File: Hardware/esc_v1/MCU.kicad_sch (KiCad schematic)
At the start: 28 parts, among them SW1 SW_Push, U4 ATSAME70J21A-AN, Y1 Crystal_GND2

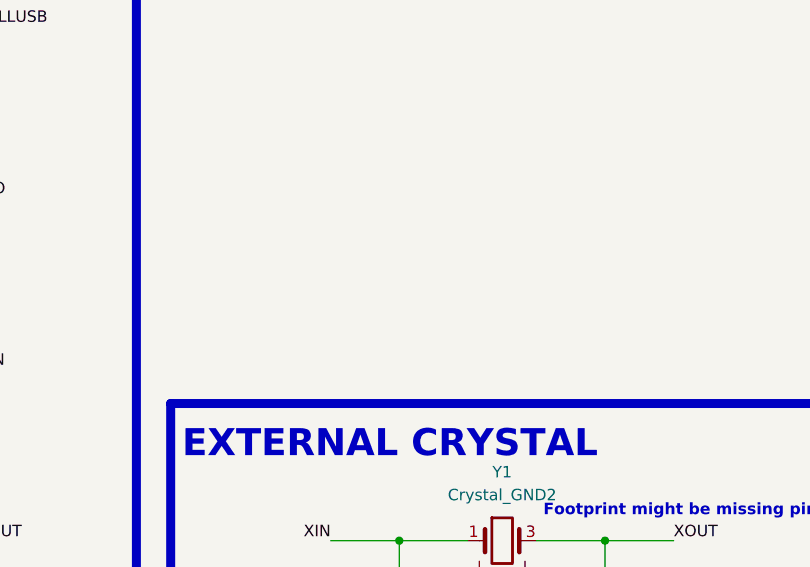
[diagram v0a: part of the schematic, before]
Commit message: changed gate driver, removed 10V buck and 5V LDO, added 5V buck. Started on Layout
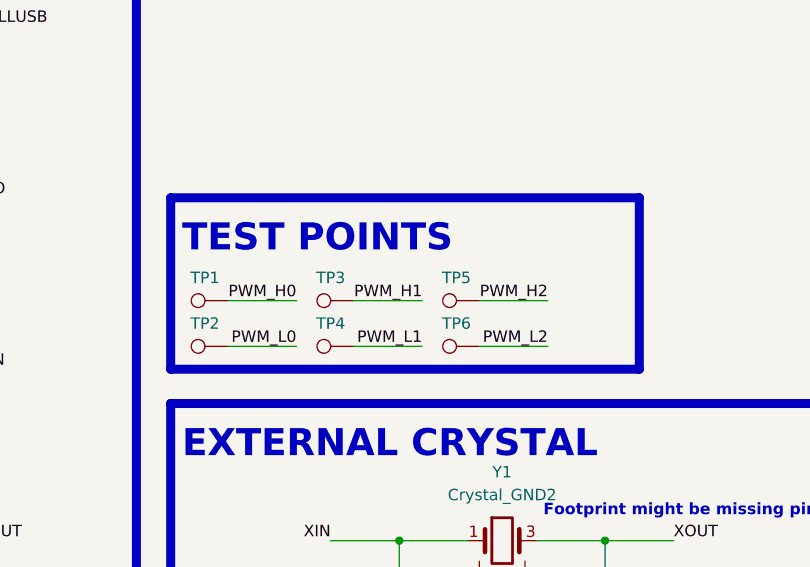
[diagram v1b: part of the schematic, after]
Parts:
- added TP1, TP2, TP3, TP4, TP5, TP6: TestPoint, TestPoint:TestPoint_Pad_D3.0mm, symbol Connector:TestPoint
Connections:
- net PWM_H0: now also TP1.1
- net PWM_H1: now also TP3.1
- net PWM_H2: now also TP5.1
- net PWM_L0: now also TP2.1
- net PWM_L1: now also TP4.1
- net PWM_L2: now also TP6.1
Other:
- note added: "TEST POINTS"
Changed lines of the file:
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@@
   (title_block
     (title "MCU")
-    (date "2022-07-21")
+    (date "2022-08-13")
     (rev "1")
   )
@@
     (stroke (width 0) (type default) (color 0 0 0 0))
   )
+  (wire (pts (xy 120.65 113.03) (xy 128.27 113.03))
+    (stroke (width 0) (type default) (color 0 0 0 0))
+  )
   (polyline (pts (xy 147.32 163.83) (xy 147.32 195.58))
     (stroke (width 1) (type solid) (color 0 0 0 0))
@@
     (stroke (width 1) (type solid) (color 0 0 0 0))
   )
+  (wire (pts (xy 134.62 118.11) (xy 142.24 118.11))
+    (stroke (width 0) (type default) (color 0 0 0 0))
+  )
   (wire (pts (xy 64.77 158.75) (xy 72.39 158.75))
     (stroke (width 0) (type default) (color 0 0 0 0))
@@
     (stroke (width 0) (type default) (color 0 0 0 0))
   )
+  (wire (pts (xy 106.68 113.03) (xy 114.3 113.03))
+    (stroke (width 0) (type default) (color 0 0 0 0))
+  )
   (polyline (pts (xy 48.26 13.97) (xy 96.52 13.97))
     (stroke (width 1) (type solid) (color 0 0 0 0))
@@
     (stroke (width 1) (type solid) (color 0 0 0 0))
   )
+  (polyline (pts (xy 152.4 120.65) (xy 100.33 120.65))
+    (stroke (width 1) (type solid) (color 0 0 0 0))
+  )
   (wire (pts (xy 73.66 34.29) (xy 74.93 34.29))
     (stroke (width 0) (type default) (color 0 0 0 0))
@@
     (stroke (width 0) (type default) (color 0 0 0 0))
   )
+  (polyline (pts (xy 152.4 101.6) (xy 100.33 101.6))
+    (stroke (width 1) (type solid) (color 0 0 0 0))
+  )
   (polyline (pts (xy 13.97 74.93) (xy 13.97 195.58))
     (stroke (width 1) (type solid) (color 0 0 0 0))
@@
     (stroke (width 0) (type default) (color 0 0 0 0))
   )
+  (wire (pts (xy 134.62 113.03) (xy 142.24 113.03))
+    (stroke (width 0) (type default) (color 0 0 0 0))
+  )
   (wire (pts (xy 118.11 139.7) (xy 125.73 139.7))
     (stroke (width 0) (type default) (color 0 0 0 0))
@@
     (stroke (width 0) (type default) (color 0 0 0 0))
   )
+  (wire (pts (xy 106.68 118.11) (xy 114.3 118.11))
+    (stroke (width 0) (type default) (color 0 0 0 0))
+  )
   (wire (pts (xy 49.53 139.7) (xy 64.77 139.7))
     (stroke (width 0) (type default) (color 0 0 0 0))
@@
     (stroke (width 1) (type solid) (color 0 0 0 0))
   )
+  (polyline (pts (xy 152.4 101.6) (xy 152.4 120.65))
+    (stroke (width 1) (type solid) (color 0 0 0 0))
+  )
   (wire (pts (xy 72.39 101.6) (xy 76.2 101.6))
     (stroke (width 0) (type default) (color 0 0 0 0))
@@
     (stroke (width 0) (type default) (color 0 0 0 0))
   )
+  (polyline (pts (xy 100.33 101.6) (xy 100.33 120.65))
+    (stroke (width 1) (type solid) (color 0 0 0 0))
+  )
   (wire (pts (xy 130.81 186.69) (xy 130.81 190.5))
     (stroke (width 0) (type default) (color 0 0 0 0))
@@
   )
   (wire (pts (xy 196.85 83.82) (xy 209.55 83.82))
+    (stroke (width 0) (type default) (color 0 0 0 0))
+  )
+  (wire (pts (xy 120.65 118.11) (xy 128.27 118.11))
     (stroke (width 0) (type default) (color 0 0 0 0))
   )
@@
     (effects (font (size 3 3) (thickness 0.6) bold) (justify left bottom))
   )
+  (text "TEST POINTS" (at 101.6 107.95 0)
+    (effects (font (size 3 3) (thickness 0.6) bold) (justify left bottom))
+  )
   (text "Footprint might be missing pin 4" (at 173.99 137.16 180)
     (effects (font (size 1.27 1.27) (thickness 0.254) bold) (justify right bottom))
@@
     (effects (font (size 1.27 1.27)) (justify left bottom))
   )
+  (label "PWM_H1" (at 128.27 113.03 180)
+    (effects (font (size 1.27 1.27)) (justify right bottom))
+  )
   (label "XOUT" (at 196.85 104.14 0)
     (effects (font (size 1.27 1.27)) (justify left bottom))
@@
     (effects (font (size 1.27 1.27)) (justify left bottom))
   )
+  (label "PWM_L2" (at 142.24 118.11 180)
+    (effects (font (size 1.27 1.27)) (justify right bottom))
+  )
   (label "VDDPLL" (at 242.57 30.48 0)
     (effects (font (size 1.27 1.27)) (justify left bottom))
@@
   (label "VDDIO" (at 227.33 20.32 0)
     (effects (font (size 1.27 1.27)) (justify left bottom))
+  )
+  (label "PWM_L0" (at 114.3 118.11 180)
+    (effects (font (size 1.27 1.27)) (justify right bottom))
+  )
+  (label "PWM_H2" (at 142.24 113.03 180)
+    (effects (font (size 1.27 1.27)) (justify right bottom))
   )
   (label "VDDOUT" (at 76.2 139.7 0)
@@
     (effects (font (size 1.27 1.27)) (justify left bottom))
   )
+  (label "PWM_H0" (at 114.3 113.03 180)
+    (effects (font (size 1.27 1.27)) (justify right bottom))
+  )
   (label "VDDCORE" (at 232.41 22.86 0)
     (effects (font (size 1.27 1.27)) (justify left bottom))
+  )
+  (label "PWM_L1" (at 128.27 118.11 180)
+    (effects (font (size 1.27 1.27)) (justify right bottom))
   )
   (label "VDDIN" (at 76.2 120.65 0)
@@
     (pin "1")
   )
+  (symbol (lib_id "Connector:TestPoint") (at 120.65 113.03 90) (unit 1)
+    (in_bom yes) (on_board yes)
+    (property "Reference" "TP3" (id 0) (at 118.11 110.49 90))
+    (property "Value" "TestPoint" (id 1) (at 118.6179 110.49 0)
+      (effects (font (size 1.27 1.27)) (justify left) hide)
+    )
+    (property "Footprint" "TestPoint:TestPoint_Pad_D3.0mm" (id 2) (at 120.65 107.95 0)
+      (effects (font (size 1.27 1.27)) hide)
+    )
+    (property "Datasheet" "~" (id 3) (at 120.65 107.95 0)
+      (effects (font (size 1.27 1.27)) hide)
+    )
+    (pin "1")
+  )
   (symbol (lib_id "power:GND") (at 72.39 167.64 0) (unit 1)
     (in_bom yes) (on_board yes) (fields_autoplaced)
@@
     (pin "1")
     (pin "2")
+  )
+  (symbol (lib_id "Connector:TestPoint") (at 120.65 118.11 90) (unit 1)
+    (in_bom yes) (on_board yes)
+    (property "Reference" "TP4" (id 0) (at 118.11 115.57 90))
+    (property "Value" "TestPoint" (id 1) (at 118.6179 115.57 0)
+      (effects (font (size 1.27 1.27)) (justify left) hide)
+    )
+    (property "Footprint" "TestPoint:TestPoint_Pad_D3.0mm" (id 2) (at 120.65 113.03 0)
+      (effects (font (size 1.27 1.27)) hide)
+    )
+    (property "Datasheet" "~" (id 3) (at 120.65 113.03 0)
+      (effects (font (size 1.27 1.27)) hide)
+    )
+    (pin "1")
   )
   (symbol (lib_id "MCU_Microchip_SAME:ATSAME70J21A-AN") (at 234.95 88.9 0) (unit 1)
@@
     (pin "9")
   )
+  (symbol (lib_id "Connector:TestPoint") (at 134.62 118.11 90) (unit 1)
+    (in_bom yes) (on_board yes)
+    (property "Reference" "TP6" (id 0) (at 132.08 115.57 90))
+    (property "Value" "TestPoint" (id 1) (at 132.5879 115.57 0)
+      (effects (font (size 1.27 1.27)) (justify left) hide)
+    )
+    (property "Footprint" "TestPoint:TestPoint_Pad_D3.0mm" (id 2) (at 134.62 113.03 0)
+      (effects (font (size 1.27 1.27)) hide)
+    )
+    (property "Datasheet" "~" (id 3) (at 134.62 113.03 0)
+      (effects (font (size 1.27 1.27)) hide)
+    )
+    (pin "1")
+  )
   (symbol (lib_id "Device:Crystal_GND2") (at 137.16 139.7 0) (unit 1)
     (in_bom yes) (on_board yes) (fields_autoplaced)
@@
     (pin "2")
   )
+  (symbol (lib_id "Connector:TestPoint") (at 106.68 118.11 90) (unit 1)
+    (in_bom yes) (on_board yes)
+    (property "Reference" "TP2" (id 0) (at 104.14 115.57 90))
+    (property "Value" "TestPoint" (id 1) (at 104.6479 115.57 0)
+      (effects (font (size 1.27 1.27)) (justify left) hide)
+    )
+    (property "Footprint" "TestPoint:TestPoint_Pad_D3.0mm" (id 2) (at 106.68 113.03 0)
+      (effects (font (size 1.27 1.27)) hide)
+    )
+    (property "Datasheet" "~" (id 3) (at 106.68 113.03 0)
+      (effects (font (size 1.27 1.27)) hide)
+    )
+    (pin "1")
+  )
   (symbol (lib_id "power:GND") (at 204.47 152.4 0) (unit 1)
     (in_bom yes) (on_board yes) (fields_autoplaced)
@@
     )
     (property "Datasheet" "" (id 3) (at 49.53 147.32 0)
+      (effects (font (size 1.27 1.27)) hide)
+    )
+    (pin "1")
+  )
+  (symbol (lib_id "Connector:TestPoint") (at 134.62 113.03 90) (unit 1)
+    (in_bom yes) (on_board yes)
+    (property "Reference" "TP5" (id 0) (at 132.08 110.49 90))
+    (property "Value" "TestPoint" (id 1) (at 132.5879 110.49 0)
+      (effects (font (size 1.27 1.27)) (justify left) hide)
+    )
+    (property "Footprint" "TestPoint:TestPoint_Pad_D3.0mm" (id 2) (at 134.62 107.95 0)
+      (effects (font (size 1.27 1.27)) hide)
+    )
+    (property "Datasheet" "~" (id 3) (at 134.62 107.95 0)
       (effects (font (size 1.27 1.27)) hide)
     )
@@
     (pin "2")
   )
+  (symbol (lib_id "Connector:TestPoint") (at 106.68 113.03 90) (unit 1)
+    (in_bom yes) (on_board yes)
+    (property "Reference" "TP1" (id 0) (at 104.14 110.49 90))
+    (property "Value" "TestPoint" (id 1) (at 104.6479 110.49 0)
+      (effects (font (size 1.27 1.27)) (justify left) hide)
+    )
+    (property "Footprint" "TestPoint:TestPoint_Pad_D3.0mm" (id 2) (at 106.68 107.95 0)
+      (effects (font (size 1.27 1.27)) hide)
+    )
+    (property "Datasheet" "~" (id 3) (at 106.68 107.95 0)
+      (effects (font (size 1.27 1.27)) hide)
+    )
+    (pin "1")
+  )
   (symbol (lib_id "Device:C_Small") (at 64.77 162.56 0) (unit 1)

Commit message: Continued on layout
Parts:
- TP1, TP2, TP3, TP4, TP5, TP6: footprint TestPoint:TestPoint_Pad_D3.0mm -> TestPoint:TestPoint_Pad_D2.0mm
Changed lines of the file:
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@@
       (effects (font (size 1.27 1.27)) (justify left) hide)
     )
-    (property "Footprint" "TestPoint:TestPoint_Pad_D3.0mm" (id 2) (at 120.65 107.95 0)
+    (property "Footprint" "TestPoint:TestPoint_Pad_D2.0mm" (id 2) (at 120.65 107.95 0)
       (effects (font (size 1.27 1.27)) hide)
     )
@@
       (effects (font (size 1.27 1.27)) (justify left) hide)
     )
-    (property "Footprint" "TestPoint:TestPoint_Pad_D3.0mm" (id 2) (at 120.65 113.03 0)
+    (property "Footprint" "TestPoint:TestPoint_Pad_D2.0mm" (id 2) (at 120.65 113.03 0)
       (effects (font (size 1.27 1.27)) hide)
     )
@@
       (effects (font (size 1.27 1.27)) (justify left) hide)
     )
-    (property "Footprint" "TestPoint:TestPoint_Pad_D3.0mm" (id 2) (at 134.62 113.03 0)
+    (property "Footprint" "TestPoint:TestPoint_Pad_D2.0mm" (id 2) (at 134.62 113.03 0)
       (effects (font (size 1.27 1.27)) hide)
     )
@@
       (effects (font (size 1.27 1.27)) (justify left) hide)
     )
-    (property "Footprint" "TestPoint:TestPoint_Pad_D3.0mm" (id 2) (at 106.68 113.03 0)
+    (property "Footprint" "TestPoint:TestPoint_Pad_D2.0mm" (id 2) (at 106.68 113.03 0)
       (effects (font (size 1.27 1.27)) hide)
     )
@@
       (effects (font (size 1.27 1.27)) (justify left) hide)
     )
-    (property "Footprint" "TestPoint:TestPoint_Pad_D3.0mm" (id 2) (at 134.62 107.95 0)
+    (property "Footprint" "TestPoint:TestPoint_Pad_D2.0mm" (id 2) (at 134.62 107.95 0)
       (effects (font (size 1.27 1.27)) hide)
     )
@@
       (effects (font (size 1.27 1.27)) (justify left) hide)
     )
-    (property "Footprint" "TestPoint:TestPoint_Pad_D3.0mm" (id 2) (at 106.68 107.95 0)
-      (effects (font (size 1.27 1.27)) hide)
-    )
+    (property "Footprint" "TestPoint:TestPoint_Pad_D2.0mm" (id 2) (at 106.68 107.95 0)
+      (effects (font (size 1.27 1.27)) hide)
+    )

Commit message: Changed to 6 layer pcb, increased space by 10mm, redid gate driver traces and power planes
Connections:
- net overcurr_err_U: now also U4.8 (PB0); no longer U4.7 (PB1)
- net overcurr_err_V: now also U4.7 (PB1); no longer U4.8 (PB0)
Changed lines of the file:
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@@
+    (effects (font (size 1.27 1.27)) (justify right))
+  )
+  (hierarchical_label "overcurr_err_V" (shape passive) (at 196.85 86.36 180)
     (effects (font (size 1.27 1.27)) (justify right))
   )
@@
     (effects (font (size 1.27 1.27)) (justify left))
   )
-  (hierarchical_label "overcurr_err_U" (shape passive) (at 196.85 86.36 180)
-    (effects (font (size 1.27 1.27)) (justify right))
-  )
   (hierarchical_label "UART0_TX" (shape passive) (at 196.85 55.88 180)
     (effects (font (size 1.27 1.27)) (justify right))
   )
-  (hierarchical_label "overcurr_err_V" (shape passive) (at 196.85 83.82 180)
+  (hierarchical_label "overcurr_err_U" (shape passive) (at 196.85 83.82 180)
     (effects (font (size 1.27 1.27)) (justify right))
   )

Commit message: Finished layout. Final check remains
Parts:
- L2: footprint Inductor_SMD:L_0201_0603Metric -> Inductor_SMD:L_0603_1608Metric
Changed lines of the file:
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@@
     (property "Reference" "L2" (id 0) (at 55.88 77.47 90))
     (property "Value" "10uH - 60mA" (id 1) (at 55.88 80.01 90))
-    (property "Footprint" "Inductor_SMD:L_0201_0603Metric" (id 2) (at 55.88 82.55 0)
+    (property "Footprint" "Inductor_SMD:L_0603_1608Metric" (id 2) (at 55.88 82.55 0)
       (effects (font (size 1.27 1.27)) hide)
     )

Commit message: Removed USB to serial chip and added serial connector. Finished layout, made production files and sent to production
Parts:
- U4: Part no (none) -> ATSAME70J21A-AN
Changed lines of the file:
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@@
+      (effects (font (size 1.27 1.27)) hide)
+    )
+    (property "Part no" "ATSAME70J21A-AN" (id 4) (at 234.95 88.9 0)
       (effects (font (size 1.27 1.27)) hide)
     )
